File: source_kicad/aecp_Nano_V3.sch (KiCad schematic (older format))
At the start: 29 parts, among them P1 CONN_IGBT, P10 FIX, P11 FIX, P12 CONN_SEL2, P13 CONN_DEP2, P14 MP3V5050, P15 FIX, P16 FIX, P17 FIX, P18 FIX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

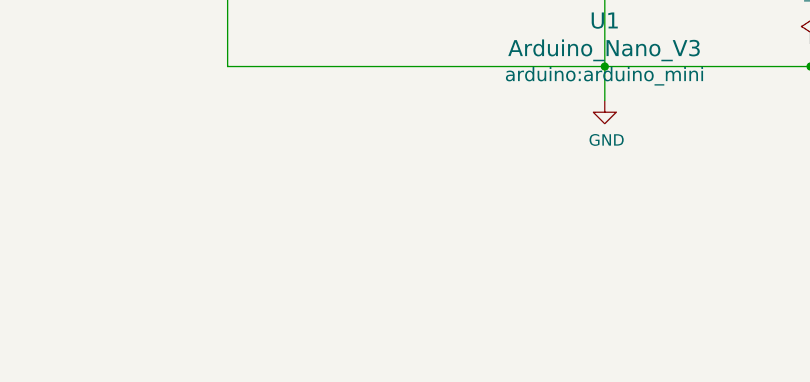
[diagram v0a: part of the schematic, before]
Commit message: New source file for kicad with bluetooth adaptator
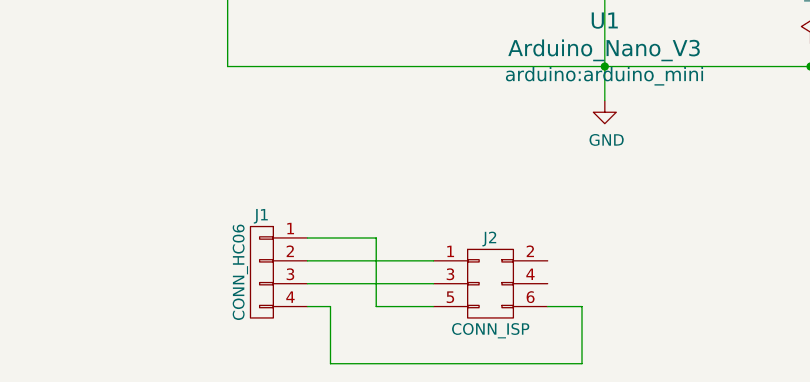
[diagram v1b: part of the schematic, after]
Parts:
- added J1: CONN_HC06, w_pin_strip:pin_strip_4, symbol CONN_01X04
- added J2: CONN_ISP, w_pin_strip:pin_strip_3x2, symbol CONN_02X03
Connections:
- new net: J1.1 (P1), J2.5 (P5)
- new net: J1.2 (P2), J2.1 (P1)
- new net: J1.3 (P3), J2.3 (P3)
- new net: J1.4 (P4), J2.6 (P6)
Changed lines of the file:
@@
 	4600 2950 4450 2950
 NoConn ~ 4450 2850
+$Comp
+L CONN_01X04 J1
+U 1 1 58CEED37
+P 2250 5500
+F 0 "J1" H 2250 5750 50  0000 C CNN
+F 1 "CONN_HC06" V 2350 5500 50  0000 C CNN
+F 2 "w_pin_strip:pin_strip_4" H 2250 5500 50  0001 C CNN
+F 3 "" H 2250 5500 50  0001 C CNN
+	1    2250 5500
+	-1   0    0    -1
+$EndComp
+$Comp
+L CONN_02X03 J2
+U 1 1 58CEEDDA
+P 3250 5550
+F 0 "J2" H 3250 5750 50  0000 C CNN
+F 1 "CONN_ISP" H 3250 5350 50  0000 C CNN
+F 2 "w_pin_strip:pin_strip_3x2" H 3250 4350 50  0001 C CNN
+F 3 "" H 3250 4350 50  0001 C CNN
+	1    3250 5550
+	1    0    0    -1
+$EndComp
+Wire Wire Line
+	2450 5650 2550 5650
+Wire Wire Line
+	2550 5650 2550 5900
+Wire Wire Line
+	2550 5900 3650 5900
+Wire Wire Line
+	3650 5900 3650 5650
+Wire Wire Line
+	3650 5650 3500 5650
+Wire Wire Line
+	2450 5550 3000 5550
+Wire Wire Line
+	2450 5450 3000 5450
+Wire Wire Line
+	2450 5350 2750 5350
+Wire Wire Line
+	2750 5350 2750 5650
+Wire Wire Line
+	2750 5650 3000 5650
 $EndSCHEMATC
